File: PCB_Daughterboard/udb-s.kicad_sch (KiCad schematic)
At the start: 10 parts, among them J1 TYPE-C-31-M-12, J2 78171-0004, U1 TPD4E05U06DQAR

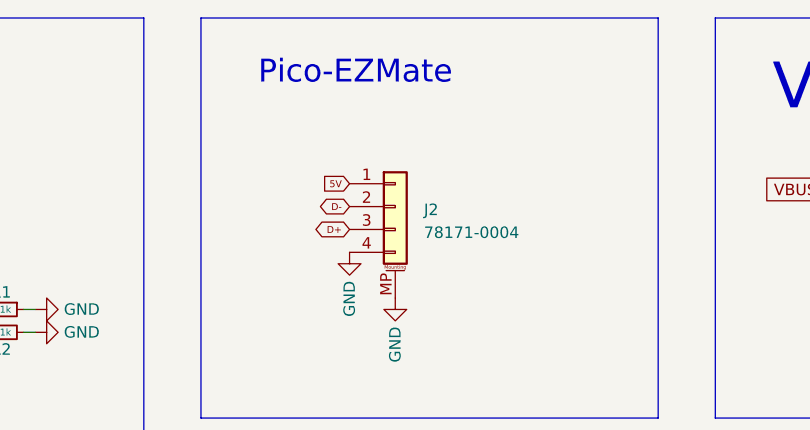
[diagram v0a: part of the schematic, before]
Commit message: Update daughterboard 3d model
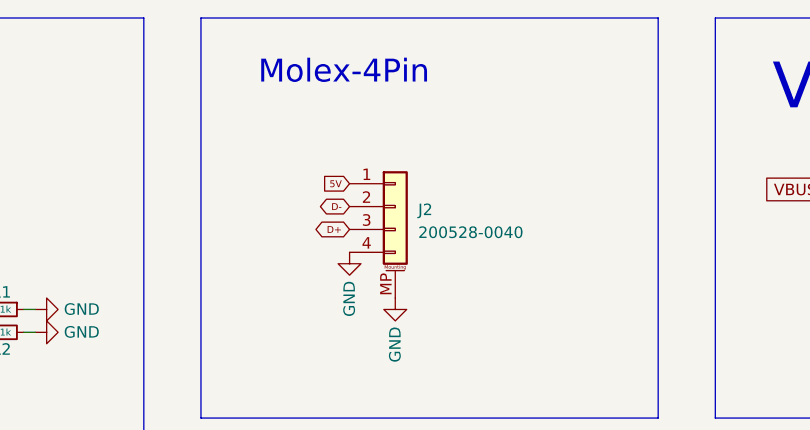
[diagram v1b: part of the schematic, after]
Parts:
- J2: value 78171-0004 -> 200528-0040
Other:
- note added: "Molex-4Pin"
- note removed: "Pico-EZMate"
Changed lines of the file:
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@@
 		)
 	)
-	(text "Pico-EZMate"
+	(text "Molex-4Pin"
 		(exclude_from_sim no)
 		(at 158.75 33.02 0)
@@
 		(fields_autoplaced yes)
 		(property "Reference" "J2"
-			(at 177.165 46.7105 0)
-			(effects
-				(font
-					(size 1.27 1.27)
-				)
-				(justify left)
-			)
-		)
-		(property "Value" "78171-0004"
-			(at 177.165 49.2505 0)
-			(effects
-				(font
+			(at 176.53 46.7105 0)
+			(effects
+				(font
+					(size 1.27 1.27)
+				)
+				(justify left)
+			)
+		)
+		(property "Value" "200528-0040"
+			(at 176.53 49.2505 0)
+			(effects
+				(font

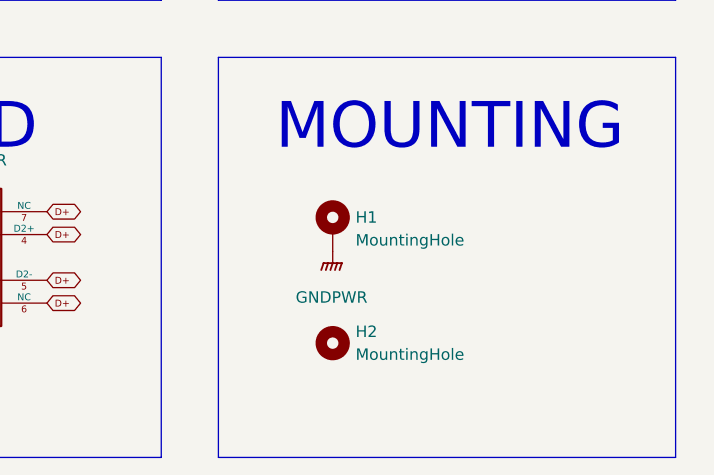
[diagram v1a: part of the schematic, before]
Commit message: Add production files
Not complete yet.
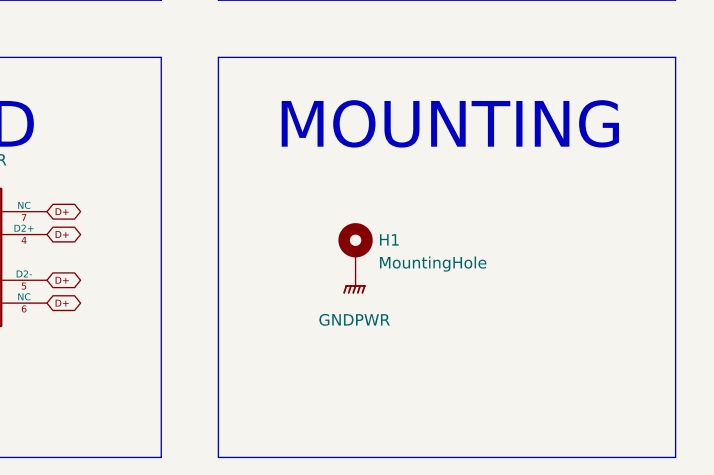
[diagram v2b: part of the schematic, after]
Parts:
- removed H2: MountingHole, MountingHole:MountingHole_3.2mm_M3_DIN965_Pad_TopOnly, symbol Mechanical:MountingHole
- FB1: footprint Inductor_SMD:L_0805_2012Metric -> Inductor_SMD:L_0805_2012Metric_Pad1.15x1.40mm_HandSolder
- H1: footprint MountingHole:MountingHole_3.2mm_M3_DIN965_Pad_TopBottom -> MountingHole:MountingHole_2.2mm_M2_Pad_TopBottom
- R1, R2: footprint Resistor_SMD:R_0402_1005Metric -> Resistor_SMD:R_0805_2012Metric_Pad1.20x1.40mm_HandSolder
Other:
- moved on the sheet: H1
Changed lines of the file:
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@@
-	)
-	(symbol
-		(lib_id "Mechanical:MountingHole")
-		(at 222.25 107.95 0)
-		(unit 1)
-		(exclude_from_sim no)
-		(in_bom no)
-		(on_board yes)
-		(dnp no)
-		(fields_autoplaced yes)
-		(property "Reference" "H2"
-			(at 224.79 106.6799 0)
-			(effects
-				(font
-					(size 1.27 1.27)
-				)
-				(justify left)
-			)
-		)
-		(property "Value" "MountingHole"
-			(at 224.79 109.2199 0)
-			(effects
-				(font
-					(size 1.27 1.27)
-				)
-				(justify left)
-			)
-		)
-		(property "Footprint" "MountingHole:MountingHole_3.2mm_M3_DIN965_Pad_TopOnly"
-			(at 222.25 107.95 0)
-			(effects
-				(font
-					(size 1.27 1.27)
-				)
-				(hide yes)
-			)
-		)
-		(property "Datasheet" "~"
-			(at 222.25 107.95 0)
-			(effects
-				(font
-					(size 1.27 1.27)
-				)
-				(hide yes)
-			)
-		)
-		(property "Description" ""
-			(at 222.25 107.95 0)
-			(effects
-				(font
-					(size 1.27 1.27)
-				)
-				(hide yes)
-			)
-		)
-		(instances
-			(project ""
-				(path "/ce236d01-874d-4ec9-8f36-59db9835f002"
-					(reference "H2")
-					(unit 1)
-				)
-			)
-		)
 	)
 	(symbol
 		(lib_id "Mechanical:MountingHole_Pad")
-		(at 222.25 95.25 0)
+		(at 224.79 97.79 0)
 		(unit 1)
 		(exclude_from_sim no)
@@
 		(fields_autoplaced yes)
 		(property "Reference" "H1"
-			(at 224.79 93.9799 0)
+			(at 227.33 96.5199 0)
 			(effects
 				(font
@@
 		)
 		(property "Value" "MountingHole"
-			(at 224.79 96.5199 0)
+			(at 227.33 99.0599 0)
 			(effects
 				(font
@@
 			)
 		)
-		(property "Footprint" "MountingHole:MountingHole_3.2mm_M3_DIN965_Pad_TopBottom"
-			(at 222.25 95.25 0)
+		(property "Footprint" "MountingHole:MountingHole_2.2mm_M2_Pad_TopBottom"
+			(at 224.79 97.79 0)
 			(effects
 				(font
@@
 		)
 		(property "Datasheet" "~"
-			(at 222.25 95.25 0)
-			(effects
-				(font
-					(size 1.27 1.27)
-				)
-				(hide yes)
-			)
-		)
-		(property "Description" ""
-			(at 222.25 95.25 0)
+			(at 224.79 97.79 0)
+			(effects
+				(font
+					(size 1.27 1.27)
+				)
+				(hide yes)
+			)
+		)
+		(property "Description" ""
+			(at 224.79 97.79 0)
 			(effects
 				(font
@@
 			)
 		)
-		(property "Footprint" "Inductor_SMD:L_0805_2012Metric"
+		(property "Footprint" "Inductor_SMD:L_0805_2012Metric_Pad1.15x1.40mm_HandSolder"
 			(at 120.777 103.505 90)
 			(effects
@@
 	(symbol
 		(lib_id "power:GNDPWR")
-		(at 222.25 97.79 0)
+		(at 224.79 100.33 0)
 		(unit 1)
 		(exclude_from_sim no)
@@
 		(fields_autoplaced yes)
 		(property "Reference" "#PWR01"
-			(at 222.25 102.87 0)
+			(at 224.79 105.41 0)
 			(effects
 				(font
@@
 		)
 		(property "Value" "GNDPWR"
-			(at 222.123 102.87 0)
+			(at 224.663 105.41 0)
 			(effects
 				(font
@@
 		)
 		(property "Footprint" ""
-			(at 222.25 99.06 0)
+			(at 224.79 101.6 0)
 			(effects
 				(font
@@
 		)
 		(property "Datasheet" ""
-			(at 222.25 99.06 0)
-			(effects
-				(font
-					(size 1.27 1.27)
-				)
-				(hide yes)
-			)
-		)
-		(property "Description" ""
-			(at 222.25 97.79 0)
+			(at 224.79 101.6 0)
+			(effects
+				(font
+					(size 1.27 1.27)
+				)
+				(hide yes)
+			)
+		)
+		(property "Description" ""
+			(at 224.79 100.33 0)
 			(effects
 				(font
@@
 			)
 		)
-		(property "Footprint" "Resistor_SMD:R_0402_1005Metric"
+		(property "Footprint" "Resistor_SMD:R_0805_2012Metric_Pad1.20x1.40mm_HandSolder"
 			(at 130.175 57.785 0)
 			(effects
@@
 			)
 		)
-		(property "Footprint" "Resistor_SMD:R_0402_1005Metric"
+		(property "Footprint" "Resistor_SMD:R_0805_2012Metric_Pad1.20x1.40mm_HandSolder"
 			(at 130.175 60.325 0)
 			(effects
